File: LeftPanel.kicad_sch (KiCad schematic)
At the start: 12 parts, among them U3 74LS596, U4 74LS596, U5 74LS596, U6 74LS596

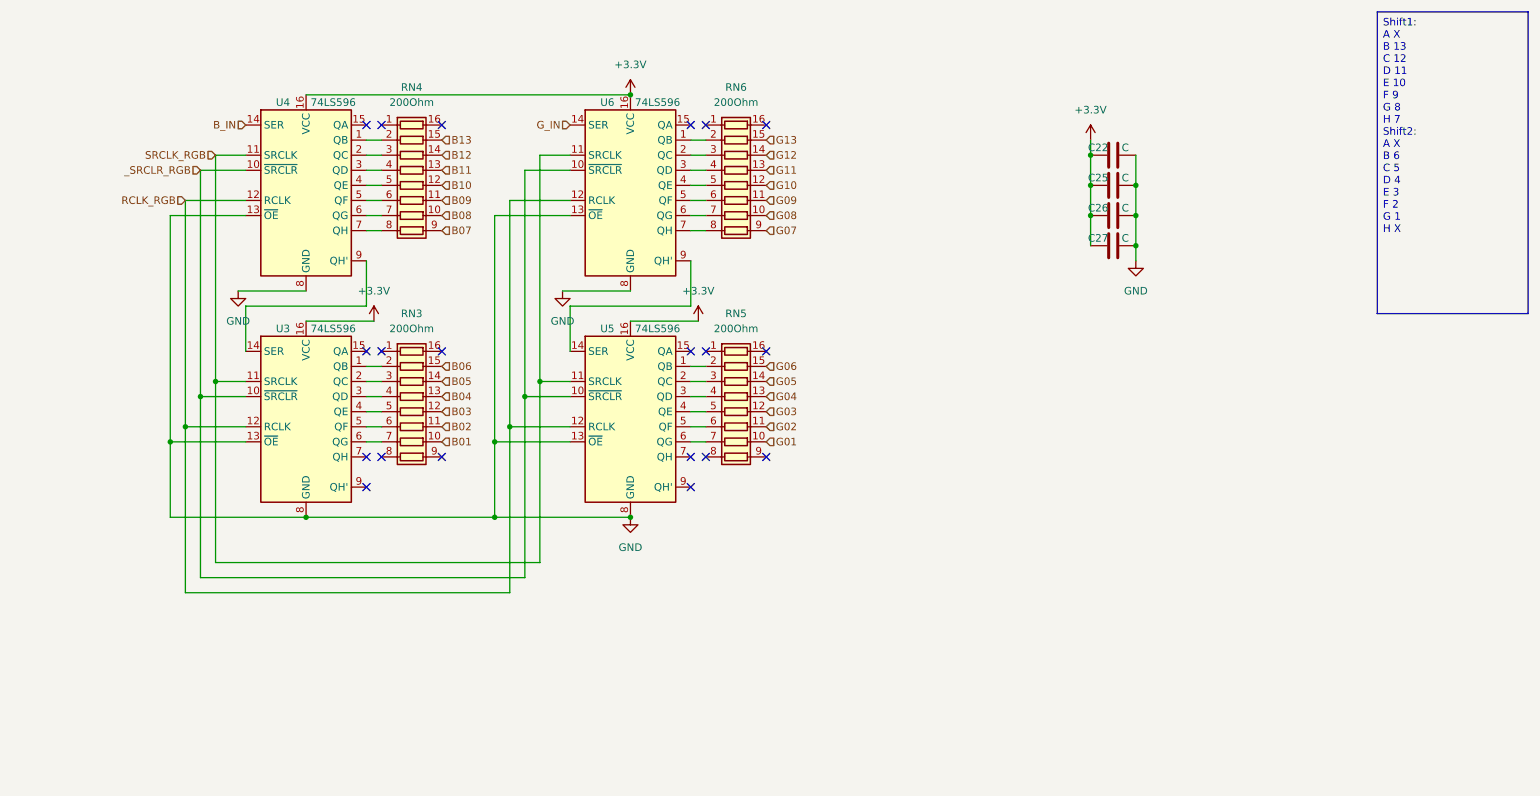
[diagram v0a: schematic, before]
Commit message: update
break down schemantic to panels, added controller and additional commponents, fixed
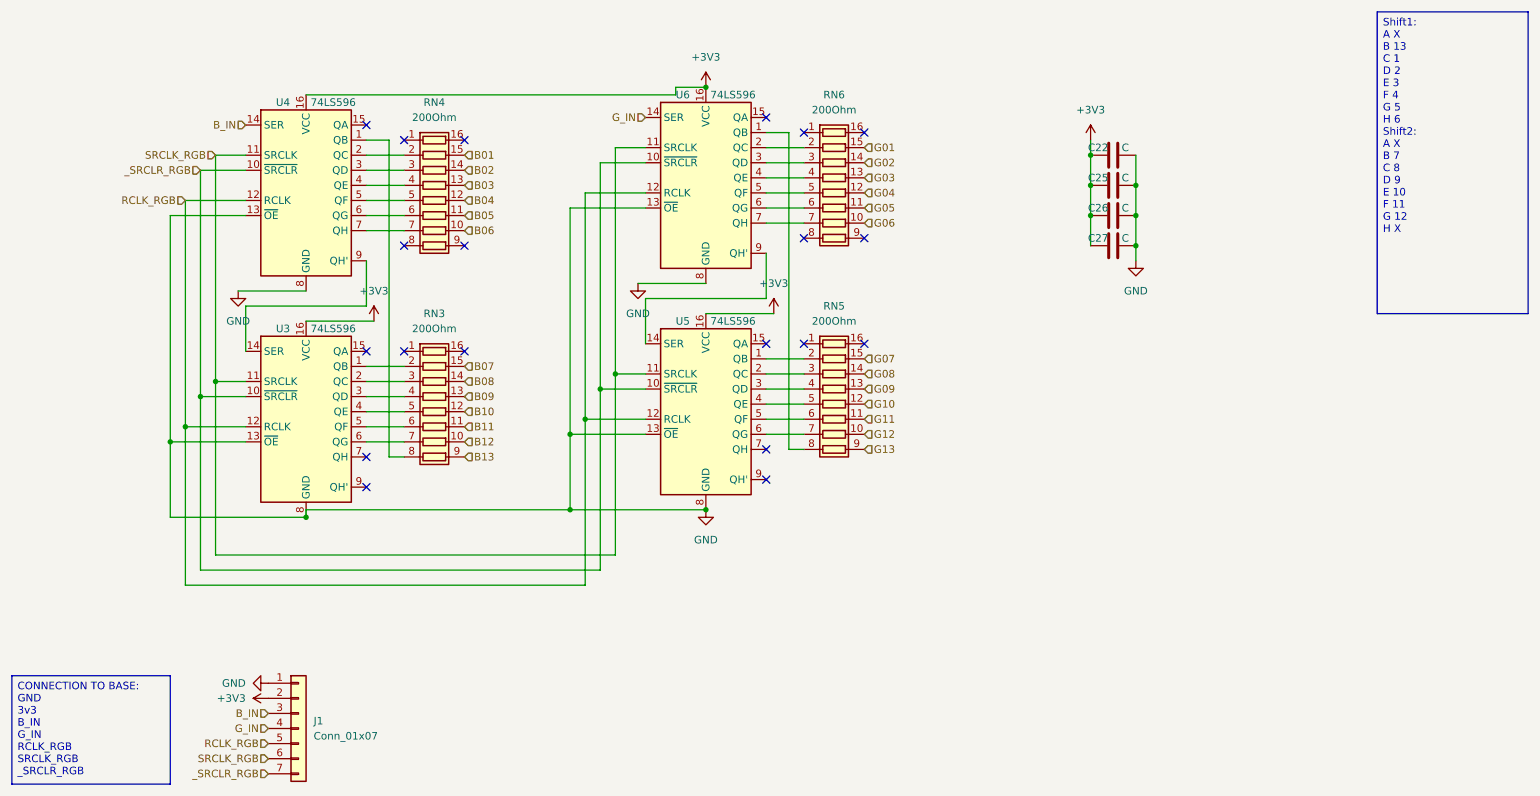
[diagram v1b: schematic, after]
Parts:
- added J1: Conn_01x07, Connector_PinSocket_2.54mm:PinSocket_1x07_P2.54mm_Vertical, symbol Connector_Generic:Conn_01x07
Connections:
- net B01: now also RN4.15 (R2.2); no longer RN3.10 (R7.2)
- net B02: now also RN4.14 (R3.2); no longer RN3.11 (R6.2)
- net B03: now also RN4.13 (R4.2); no longer RN3.12 (R5.2)
- net B04: now also RN4.12 (R5.2); no longer RN3.13 (R4.2)
- net B05: now also RN4.11 (R6.2); no longer RN3.14 (R3.2)
- net B06: now also RN4.10 (R7.2); no longer RN3.15 (R2.2)
- net B07: now also RN3.15 (R2.2); no longer RN4.9 (R8.2)
- net B08: now also RN3.14 (R3.2); no longer RN4.10 (R7.2)
- net B09: now also RN3.13 (R4.2); no longer RN4.11 (R6.2)
- net B10: now also RN3.12 (R5.2); no longer RN4.12 (R5.2)
- net B11: now also RN3.11 (R6.2); no longer RN4.13 (R4.2)
- net B12: now also RN3.10 (R7.2); no longer RN4.14 (R3.2)
- net B13: now also RN3.9 (R8.2); no longer RN4.15 (R2.2)
- net B_IN: now also J1.3 (Pin_3)
- net G01: now also RN6.15 (R2.2); no longer RN5.10 (R7.2)
- net G02: now also RN6.14 (R3.2); no longer RN5.11 (R6.2)
- net G03: now also RN6.13 (R4.2); no longer RN5.12 (R5.2)
- net G04: now also RN6.12 (R5.2); no longer RN5.13 (R4.2)
- net G05: now also RN6.11 (R6.2); no longer RN5.14 (R3.2)
- net G06: now also RN6.10 (R7.2); no longer RN5.15 (R2.2)
- net G07: now also RN5.15 (R2.2); no longer RN6.9 (R8.2)
- net G08: now also RN5.14 (R3.2); no longer RN6.10 (R7.2)
- net G09: now also RN5.13 (R4.2); no longer RN6.11 (R6.2)
- net G10: now also RN5.12 (R5.2); no longer RN6.12 (R5.2)
- net G11: now also RN5.11 (R6.2); no longer RN6.13 (R4.2)
- net G12: now also RN5.10 (R7.2); no longer RN6.14 (R3.2)
- net G13: now also RN5.9 (R8.2); no longer RN6.15 (R2.2)
- net GND: now also J1.1 (Pin_1)
- net G_IN: now also J1.4 (Pin_4)
- net RCLK_RGB: now also J1.5 (Pin_5)
- net SRCLK_RGB: now also J1.6 (Pin_6)
- net _SRCLR_RGB: now also J1.7 (Pin_7)
- net at RN5.8 (R8.1): now also U6.1 (QB)
- net at U4.1 (QB): now also RN3.8 (R8.1); no longer RN4.2 (R2.1)
- net at U4.2 (QC): now also RN4.2 (R2.1); no longer RN4.3 (R3.1)
- net at U4.3 (QD): now also RN4.3 (R3.1); no longer RN4.4 (R4.1)
- net at U4.4 (QE): now also RN4.4 (R4.1); no longer RN4.5 (R5.1)
- net at U4.5 (QF): now also RN4.5 (R5.1); no longer RN4.6 (R6.1)
- net at U4.6 (QG): now also RN4.6 (R6.1); no longer RN4.7 (R7.1)
- net at U4.7 (QH): now also RN4.7 (R7.1); no longer RN4.8 (R8.1)
- net at RN6.2 (R2.1): now also U6.2 (QC); no longer U6.1 (QB)
- net at RN6.3 (R3.1): now also U6.3 (QD); no longer U6.2 (QC)
- net at RN6.4 (R4.1): now also U6.4 (QE); no longer U6.3 (QD)
- net at RN6.5 (R5.1): now also U6.5 (QF); no longer U6.4 (QE)
- net at RN6.6 (R6.1): now also U6.6 (QG); no longer U6.5 (QF)
- net at RN6.7 (R7.1): now also U6.7 (QH); no longer U6.6 (QG)
- net at RN6.8 (R8.1): no longer U6.7 (QH)
- net +3.3V renamed +3V3
- net +3V3: now also J1.2 (Pin_2)
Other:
- moved on the sheet: RN3, RN5, U5, U6
